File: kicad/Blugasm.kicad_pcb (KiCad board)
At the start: 2 copper layers, 63.5 x 99.1 mm, 74 parts, among them J1 PWR, J2 BAT, J3 I2C, J4 OLED, J5 MOTOR, J6 USB_B_Micro, J7 PROG, Q1 DMG3415U, Q2 PHB32N06LT,118, Q3 SS8050-G, Q4 SS8050-G, SW1 PWR, SW2 PEC11R-4220K-S0024, U1 MP3V5050GP, U2 MCP73831-2-OT, U3 AP2112K-3.3, U4 MCP6001-OT, U5 CP2102N-A02-GQFN24, U6 ESP32-WROOM-32E

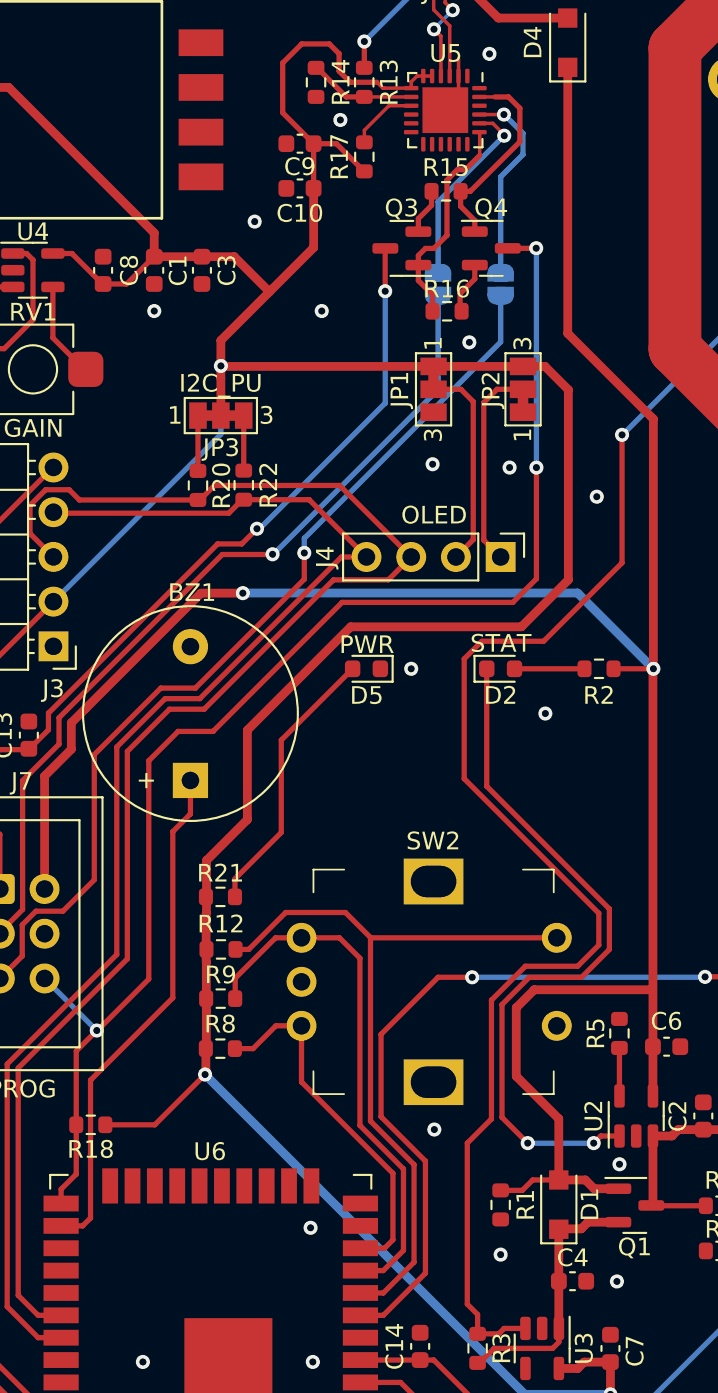
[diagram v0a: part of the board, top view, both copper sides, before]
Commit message: fix incorrect footprint
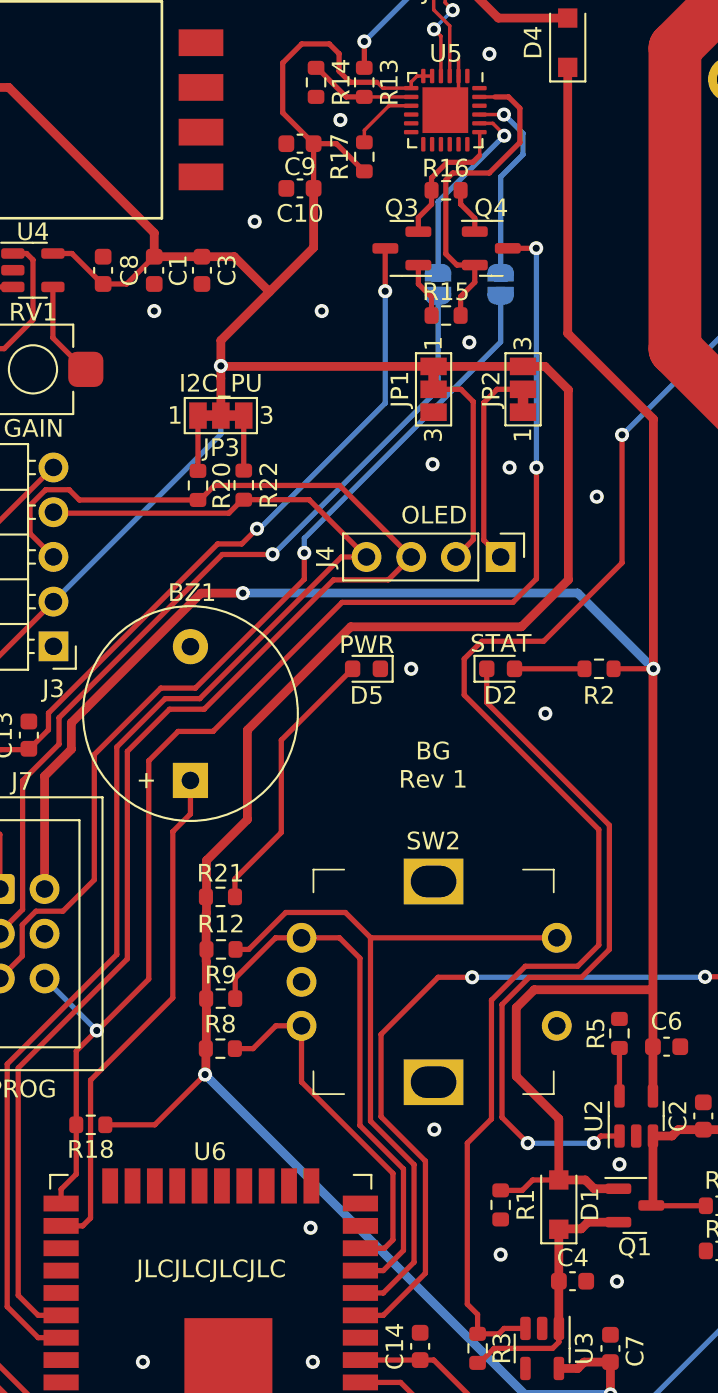
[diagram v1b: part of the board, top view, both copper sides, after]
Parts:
- moved R15 7.06 mm to (108.7, 75.2)
- moved R16 6.87 mm to (108.7, 68.1)
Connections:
- Q3 pad 1: /Controller/RTS -> Net-(Q3-Pad1)
- Q3 pad 2: Net-(Q3-Pad2) -> /Controller/RTS
- Q4 pad 1: /Controller/DTR -> Net-(Q4-Pad1)
- Q4 pad 2: Net-(Q4-Pad2) -> /Controller/DTR
- R15 pad 2: Net-(Q3-Pad2) -> Net-(Q3-Pad1)
- R16 pad 2: Net-(Q4-Pad2) -> Net-(Q4-Pad1)
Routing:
- net /Controller/DTR: track 11.6 -> 18.9 mm
- net /Controller/RTS: track 12.5 -> 7.95 mm
- net Net-(Q3-Pad1): track 0.00 -> 3.17 mm
- net Net-(Q4-Pad2): track 3.01 -> 0.00 mm
- net Net-(Q4-Pad1): track 0.00 -> 2.68 mm
- net Net-(Q3-Pad2): track 2.60 -> 0.00 mm
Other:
- board text added: "BG Rev 1"
- board text added: "JLCJLCJLCJLC"

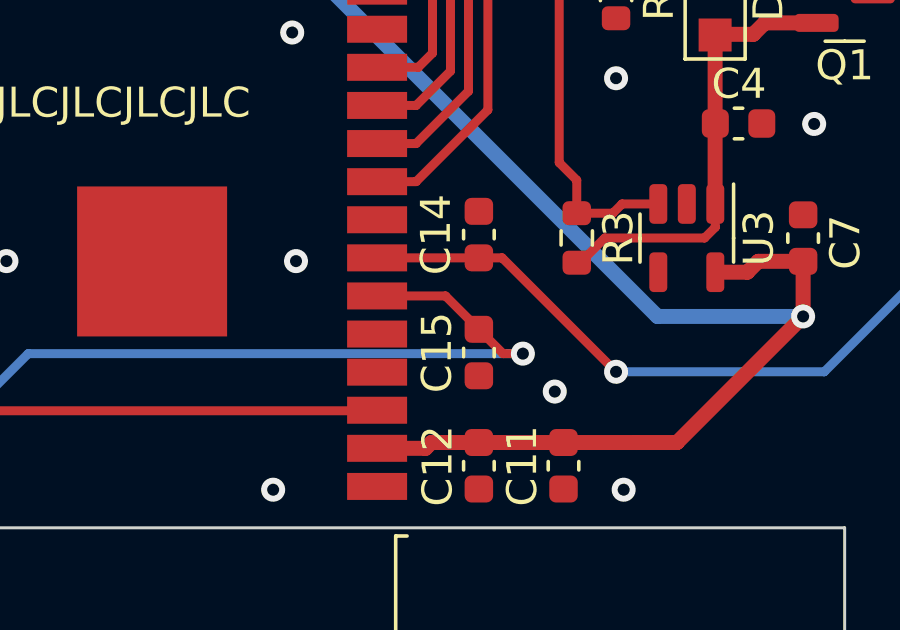
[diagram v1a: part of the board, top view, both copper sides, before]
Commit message: use sensor_vp/vn for ADC
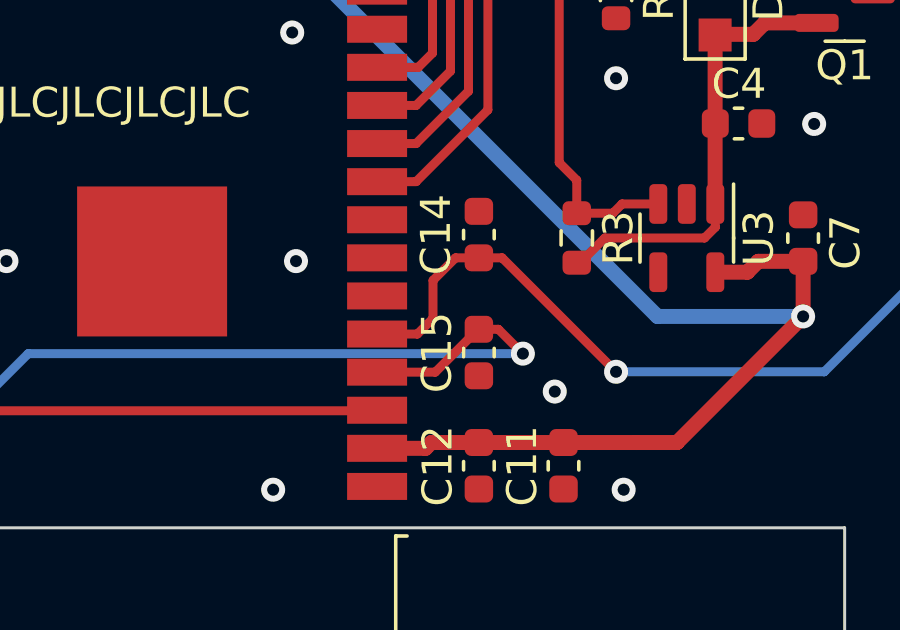
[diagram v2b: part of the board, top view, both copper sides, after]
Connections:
- U6 pad 4: unconnected-(U6-Pad4) -> /P_SENSE
- U6 pad 5: unconnected-(U6-Pad5) -> /VBAT_SENSE
- U6 pad 6: /P_SENSE -> unconnected-(U6-Pad6)
- U6 pad 7: /VBAT_SENSE -> unconnected-(U6-Pad7)
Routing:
- net /VBAT_SENSE: track 31.7 -> 33.5 mm
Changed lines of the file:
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@@
   (net 78 "Net-(JP3-Pad3)")
   (net 79 "Net-(R5-Pad1)")
-  (net 80 "unconnected-(U6-Pad5)")
+  (net 80 "unconnected-(U6-Pad6)")
   (net 81 "unconnected-(U6-Pad27)")
   (net 82 "unconnected-(U6-Pad28)")
@@
   (net 88 "Net-(JP5-Pad1)")
   (net 89 "Net-(R23-Pad1)")
-  (net 90 "unconnected-(U6-Pad4)")
+  (net 90 "unconnected-(U6-Pad7)")
   (net 91 "unconnected-(U6-Pad37)")
   (net 92 "unconnected-(U6-Pad8)")
@@
       (net 11 "/Controller/EN") (pinfunction "EN") (pintype "input"))
     (pad "4" smd rect locked (at -8.5 -4.445 180) (size 2 0.9) (layers "F.Cu" "F.Paste" "F.Mask")
-      (net 90 "unconnected-(U6-Pad4)") (pinfunction "SENSOR_VP") (pintype "input+no_connect"))
+      (net 35 "/P_SENSE") (pinfunction "SENSOR_VP") (pintype "input"))
     (pad "5" smd rect locked (at -8.5 -3.175 180) (size 2 0.9) (layers "F.Cu" "F.Paste" "F.Mask")
-      (net 80 "unconnected-(U6-Pad5)") (pinfunction "SENSOR_VN") (pintype "input+no_connect"))
+      (net 13 "/VBAT_SENSE") (pinfunction "SENSOR_VN") (pintype "input"))
     (pad "6" smd rect locked (at -8.5 -1.905 180) (size 2 0.9) (layers "F.Cu" "F.Paste" "F.Mask")
-      (net 35 "/P_SENSE") (pinfunction "IO34") (pintype "input"))
+      (net 80 "unconnected-(U6-Pad6)") (pinfunction "IO34") (pintype "input+no_connect"))
     (pad "7" smd rect locked (at -8.5 -0.635 180) (size 2 0.9) (layers "F.Cu" "F.Paste" "F.Mask")
-      (net 13 "/VBAT_SENSE") (pinfunction "IO35") (pintype "input"))
+      (net 90 "unconnected-(U6-Pad7)") (pinfunction "IO35") (pintype "input+no_connect"))
     (pad "8" smd rect locked (at -8.5 0.635 180) (size 2 0.9) (layers "F.Cu" "F.Paste" "F.Mask")
       (net 92 "unconnected-(U6-Pad8)") (pinfunction "IO32") (pintype "bidirectional+no_connect"))
@@
   (segment (start 107.188 134.511394) (end 107.962375 134.511394) (width 0.3) (layer "F.Cu") (net 13))
   (segment (start 111.76 138.309019) (end 111.76 138.309318) (width 0.3) (layer "F.Cu") (net 13))
+  (segment (start 105.659023 136.53093) (end 105.659023 135.262838) (width 0.3) (layer "F.Cu") (net 13))
   (segment (start 125.055015 128.247532) (end 125.055015 129.728069) (width 0.3) (layer "F.Cu") (net 13))
+  (segment (start 105.659023 135.262838) (end 106.410467 134.511394) (width 0.3) (layer "F.Cu") (net 13))
   (segment (start 125.055015 128.247532) (end 125.055015 125.75796) (width 0.3) (layer "F.Cu") (net 13))
-  (segment (start 103.795268 134.511394) (end 107.188 134.511394) (width 0.3) (layer "F.Cu") (net 13))
+  (segment (start 106.410467 134.511394) (end 107.188 134.511394) (width 0.3) (layer "F.Cu") (net 13))
   (segment (start 125.055015 125.75796) (end 125.065058 125.747917) (width 0.3) (layer "F.Cu") (net 13))
+  (segment (start 105.138559 137.051394) (end 105.659023 136.53093) (width 0.3) (layer "F.Cu") (net 13))
   (segment (start 107.962375 134.511394) (end 111.76 138.309019) (width 0.3) (layer "F.Cu") (net 13))
+  (segment (start 103.795268 137.051394) (end 105.138559 137.051394) (width 0.3) (layer "F.Cu") (net 13))
   (via (at 111.76 138.309318) (size 0.8) (drill 0.4) (layers "F.Cu" "B.Cu") (net 13))
   (via (at 125.047777 129.735307) (size 0.8) (drill 0.4) (layers "F.Cu" "B.Cu") (net 13))
@@
   (segment (start 100.607173 87.839662) (end 100.607173 88.669574) (width 0.3) (layer "B.Cu") (net 29))
   (segment (start 111.76 76.686835) (end 100.607173 87.839662) (width 0.3) (layer "B.Cu") (net 29))
-  (segment (start 107.188 136.899279) (end 107.993135 137.704414) (width 0.3) (layer "F.Cu") (net 35))
-  (segment (start 107.188 136.893) (end 107.188 136.899279) (width 0.3) (layer "F.Cu") (net 35))
-  (segment (start 107.188 136.893) (end 106.076394 135.781394) (width 0.3) (layer "F.Cu") (net 35))
+  (segment (start 108.649435 137.704414) (end 108.654593 137.704414) (width 0.3) (layer "F.Cu") (net 35))
+  (segment (start 105.734792 138.321394) (end 107.163186 136.893) (width 0.3) (layer "F.Cu") (net 35))
+  (segment (start 103.795268 138.321394) (end 105.734792 138.321394) (width 0.3) (layer "F.Cu") (net 35))
   (segment (start 82.756675 141.095193) (end 83.926986 141.095193) (width 0.3) (layer "F.Cu") (net 35))
   (segment (start 77.696983 133.413) (end 77.696983 136.035501) (width 0.3) (layer "F.Cu") (net 35))
-  (segment (start 107.993135 137.704414) (end 108.654593 137.704414) (width 0.3) (layer "F.Cu") (net 35))
+  (segment (start 107.163186 136.893) (end 107.188 136.893) (width 0.3) (layer "F.Cu") (net 35))
   (segment (start 77.696983 136.035501) (end 82.756675 141.095193) (width 0.3) (layer "F.Cu") (net 35))
-  (segment (start 106.076394 135.781394) (end 103.795268 135.781394) (width 0.3) (layer "F.Cu") (net 35))
+  (segment (start 107.188 136.893) (end 107.838021 136.893) (width 0.3) (layer "F.Cu") (net 35))
+  (segment (start 107.838021 136.893) (end 108.649435 137.704414) (width 0.3) (layer "F.Cu") (net 35))
   (via (at 83.926986 141.095193) (size 0.8) (drill 0.4) (layers "F.Cu" "B.Cu") (net 35))
   (via (at 108.654593 137.704414) (size 0.8) (drill 0.4) (layers "F.Cu" "B.Cu") (net 35))
